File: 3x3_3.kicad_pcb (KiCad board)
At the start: 2 copper layers, 75 x 75 mm, 24 parts, among them J1 Conn_01x01_Male, SW1 SW_Push, SW2 SW_Push, SW3 SW_Push, SW4 SW_Push, SW5 SW_Push, SW6 SW_Push, SW7 SW_Push, SW8 SW_Push, SW9 SW_Push

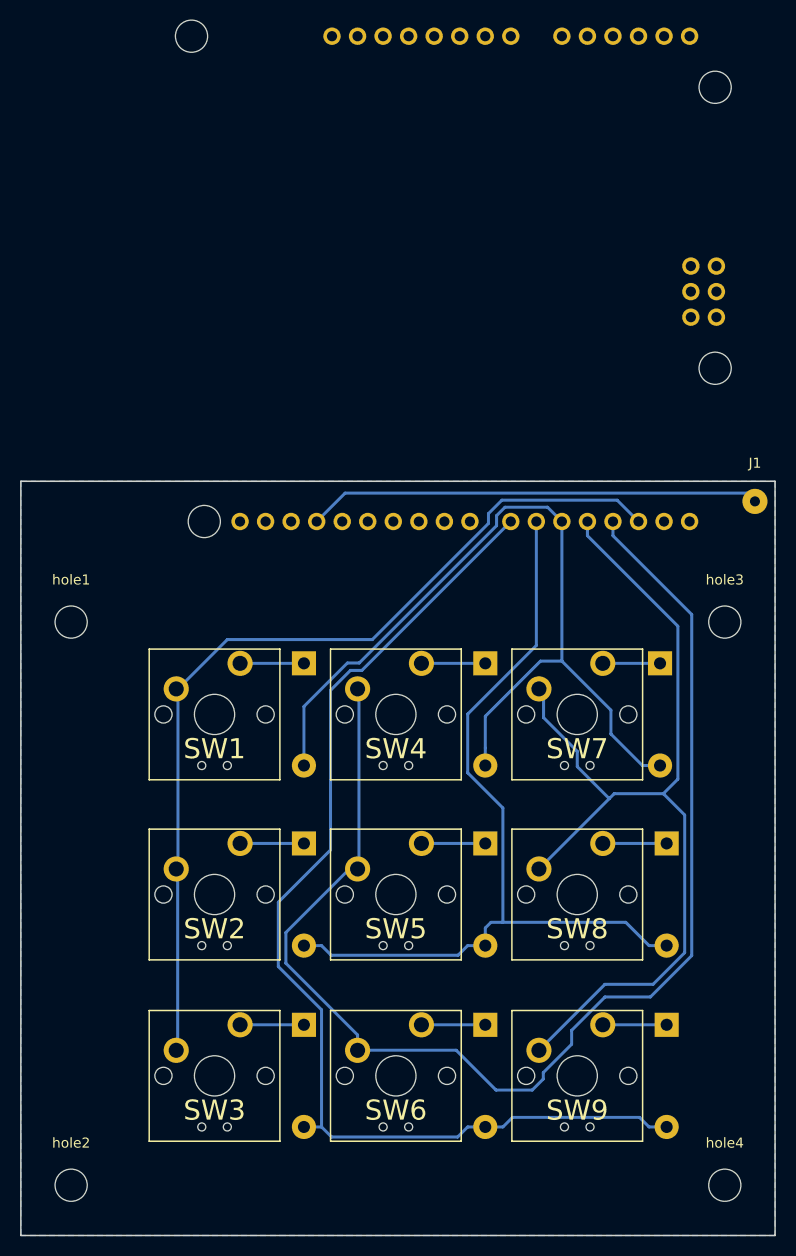
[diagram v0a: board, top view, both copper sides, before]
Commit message: クリアランスと太さを0.3に
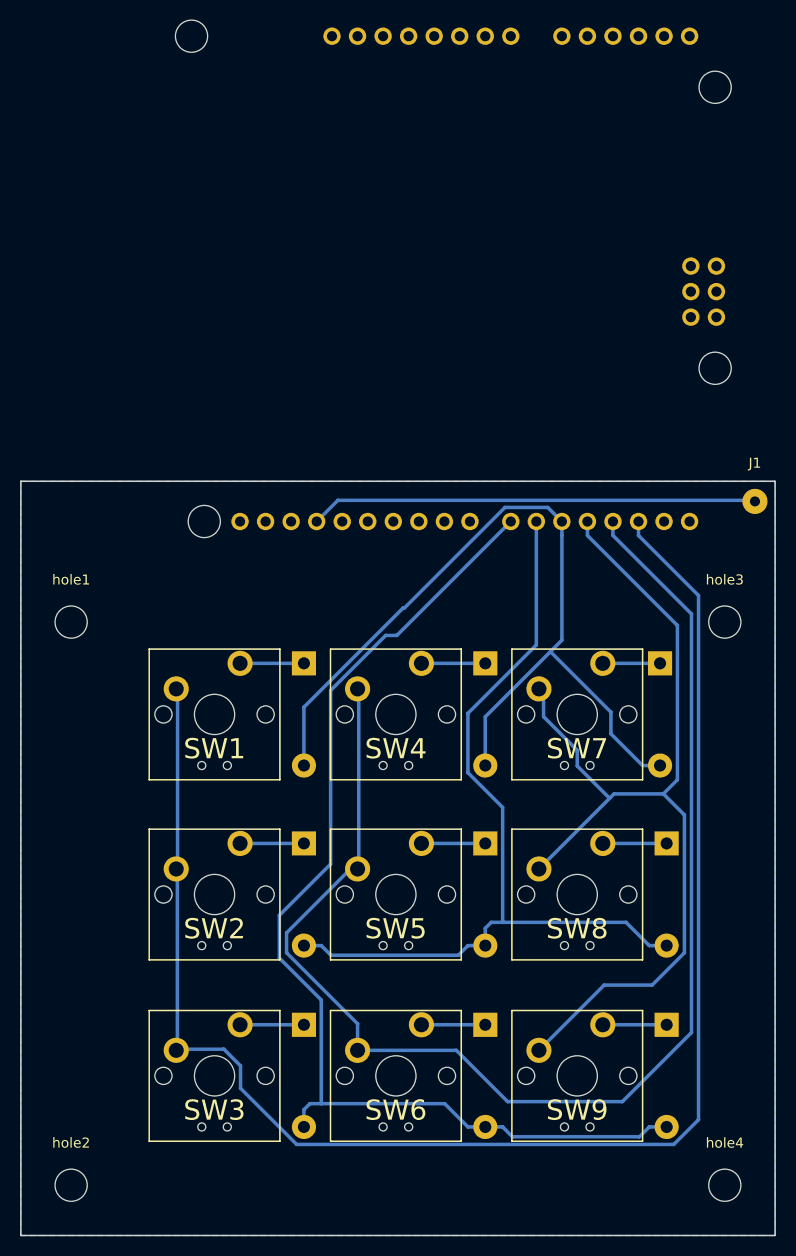
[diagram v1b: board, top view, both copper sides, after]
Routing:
- net /col0: track 91.3 -> 156.2 mm
- net /col1: track 130.4 -> 134.5 mm
- net GND: track 45.1 -> 44.5 mm
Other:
- net class Default: clearance 0.4 -> 0.35; trace_width 0.3 -> 0.35
- rule trace_clearance: 0.4 -> 0.35
